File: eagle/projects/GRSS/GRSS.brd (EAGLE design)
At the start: 76 x 39 mm, 24 parts, among them J1 MOL-SL-2-RA, J10 MOL-SL-2-RA, J11 M02PTH, J2 MOL-SL-2-RA, J3 MOL-SL-2-RA, J4 MOL-SL-2-RA, J5 MOL-SL-2-RA, J6 MOL-SL-2-RA, J7 MOL-SL-2-RA, J8 MOL-SL-2-RA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

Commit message: board update rq
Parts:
- moved C2 9.49 mm to (60.8, 8.07)
- moved C3 9.06 mm to (60.7, 6.34)
- moved U2 3.00 mm to (66.1, 7.39)
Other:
- board size 76 x 39 mm -> 85 x 47 mm
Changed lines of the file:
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@@
 <board>
 <plain>
-<wire x1="0" y1="0" x2="76" y2="0" width="0" layer="20"/>
-<wire x1="76" y1="0" x2="76" y2="39" width="0" layer="20"/>
-<wire x1="76" y1="39" x2="0" y2="39" width="0" layer="20"/>
-<wire x1="0" y1="39" x2="0" y2="0" width="0" layer="20"/>
+<wire x1="0" y1="0" x2="85" y2="0" width="0" layer="20"/>
+<wire x1="85" y1="0" x2="85" y2="47" width="0" layer="20"/>
+<wire x1="85" y1="47" x2="0" y2="47" width="0" layer="20"/>
+<wire x1="0" y1="47" x2="0" y2="0" width="0" layer="20"/>
 </plain>
 <attributes>
@@
 <attribute name="TOLERANCE" value="10%" x="69.704" y="25.944" size="1.778" layer="27" display="off"/>
 </element>
-<element name="C2" library="grss" package="C0603" value="10uF" x="69.756" y="5.072">
-<attribute name="VENDOR_PN" value="490-10474-1-ND" x="69.756" y="5.072" size="1.778" layer="27" display="off"/>
-<attribute name="VENDOR" value="Digi-key" x="69.756" y="5.072" size="1.778" layer="27" display="off"/>
-<attribute name="MANUFACTURER" value="Murata" x="69.756" y="5.072" size="1.778" layer="27" display="off"/>
-<attribute name="VOLTAGE" value="10V" x="69.756" y="5.072" size="1.778" layer="27" display="off"/>
-<attribute name="MANUFACTURER_PN" value="GRM188R61A106KE69D" x="69.756" y="5.072" size="1.778" layer="27" display="off"/>
-<attribute name="TEMP_COEFF" value="X5R" x="69.756" y="5.072" size="1.778" layer="27" display="off"/>
-<attribute name="TOLERANCE" value="10%" x="69.756" y="5.072" size="1.778" layer="27" display="off"/>
-</element>
-<element name="C3" library="grss" package="C0603" value="2.2uF" x="69.74" y="7.342">
-<attribute name="VENDOR_PN" value="490-3296-1-ND" x="69.74" y="7.342" size="1.778" layer="27" display="off"/>
-<attribute name="VENDOR" value="Digi-key" x="69.74" y="7.342" size="1.778" layer="27" display="off"/>
-<attribute name="MANUFACTURER" value="Murata" x="69.74" y="7.342" size="1.778" layer="27" display="off"/>
-<attribute name="VOLTAGE" value="16V" x="69.74" y="7.342" size="1.778" layer="27" display="off"/>
-<attribute name="MANUFACTURER_PN" value="GRM188R61C225KE15D" x="69.74" y="7.342" size="1.778" layer="27" display="off"/>
-<attribute name="TEMP_COEFF" value="X5R" x="69.74" y="7.342" size="1.778" layer="27" display="off"/>
-<attribute name="TOLERANCE" value="10%" x="69.74" y="7.342" size="1.778" layer="27" display="off"/>
+<element name="C2" library="grss" package="C0603" value="10uF" x="60.756" y="8.072">
+<attribute name="VENDOR_PN" value="490-10474-1-ND" x="60.756" y="8.072" size="1.778" layer="27" display="off"/>
+<attribute name="VENDOR" value="Digi-key" x="60.756" y="8.072" size="1.778" layer="27" display="off"/>
+<attribute name="MANUFACTURER" value="Murata" x="60.756" y="8.072" size="1.778" layer="27" display="off"/>
+<attribute name="VOLTAGE" value="10V" x="60.756" y="8.072" size="1.778" layer="27" display="off"/>
+<attribute name="MANUFACTURER_PN" value="GRM188R61A106KE69D" x="60.756" y="8.072" size="1.778" layer="27" display="off"/>
+<attribute name="TEMP_COEFF" value="X5R" x="60.756" y="8.072" size="1.778" layer="27" display="off"/>
+<attribute name="TOLERANCE" value="10%" x="60.756" y="8.072" size="1.778" layer="27" display="off"/>
+</element>
+<element name="C3" library="grss" package="C0603" value="2.2uF" x="60.74" y="6.342">
+<attribute name="VENDOR_PN" value="490-3296-1-ND" x="60.74" y="6.342" size="1.778" layer="27" display="off"/>
+<attribute name="VENDOR" value="Digi-key" x="60.74" y="6.342" size="1.778" layer="27" display="off"/>
+<attribute name="MANUFACTURER" value="Murata" x="60.74" y="6.342" size="1.778" layer="27" display="off"/>
+<attribute name="VOLTAGE" value="16V" x="60.74" y="6.342" size="1.778" layer="27" display="off"/>
+<attribute name="MANUFACTURER_PN" value="GRM188R61C225KE15D" x="60.74" y="6.342" size="1.778" layer="27" display="off"/>
+<attribute name="TEMP_COEFF" value="X5R" x="60.74" y="6.342" size="1.778" layer="27" display="off"/>
+<attribute name="TOLERANCE" value="10%" x="60.74" y="6.342" size="1.778" layer="27" display="off"/>
 </element>
 <element name="C4" library="grss" package="C0603" value="1uF" x="69.74" y="9.628">
@@
 <attribute name="TOLERANCE" value="1%" x="69.66" y="14.184" size="1.778" layer="27" display="off"/>
 </element>
-<element name="U2" library="grss" package="M08A" value="LMC555CMX/NOPB" x="63.09" y="7.39">
-<attribute name="VENDOR_PN" value="LMC555CMX/NOPBCT-ND" x="63.09" y="7.39" size="1.778" layer="27" display="off"/>
-<attribute name="VENDOR" value="Digi-key" x="63.09" y="7.39" size="1.778" layer="27" display="off"/>
-<attribute name="MANUFACTURER" value="Texas Instruments" x="63.09" y="7.39" size="1.778" layer="27" display="off"/>
-<attribute name="MANUFACTURER_PN" value="LMC555CMX/NOPB" x="63.09" y="7.39" size="1.778" layer="27" display="off"/>
+<element name="U2" library="grss" package="M08A" value="LMC555CMX/NOPB" x="66.09" y="7.39">
+<attribute name="VENDOR_PN" value="LMC555CMX/NOPBCT-ND" x="66.09" y="7.39" size="1.778" layer="27" display="off"/>
+<attribute name="VENDOR" value="Digi-key" x="66.09" y="7.39" size="1.778" layer="27" display="off"/>
+<attribute name="MANUFACTURER" value="Texas Instruments" x="66.09" y="7.39" size="1.778" layer="27" display="off"/>
+<attribute name="MANUFACTURER_PN" value="LMC555CMX/NOPB" x="66.09" y="7.39" size="1.778" layer="27" display="off"/>
 </element>
 <element name="U3" library="grss" package="MF05A" value="LP2985AIM5-4.5/NOPB" x="62.77" y="31.12">
@@
 <contactref element="U2" pad="8"/>
 <contactref element="U3" pad="5"/>
-<wire x1="65.5538" y1="9.295" x2="68.89" y2="7.342" width="0" layer="19" extent="1-1"/>
-<wire x1="65.5538" y1="8.025" x2="65.5538" y2="9.295" width="0" layer="19" extent="1-1"/>
-<wire x1="60.6262" y1="5.485" x2="65.5538" y2="8.025" width="0" layer="19" extent="1-1"/>
-<wire x1="70.51" y1="14.184" x2="65.5538" y2="9.295" width="0" layer="19" extent="1-1"/>
-<wire x1="63.9892" y1="32.0725" x2="60.6262" y2="5.485" width="0" layer="19" extent="1-1"/>
+<wire x1="68.5538" y1="9.295" x2="59.89" y2="6.342" width="0" layer="19" extent="1-1"/>
+<wire x1="68.5538" y1="8.025" x2="68.5538" y2="9.295" width="0" layer="19" extent="1-1"/>
+<wire x1="63.6262" y1="5.485" x2="68.5538" y2="8.025" width="0" layer="19" extent="1-1"/>
+<wire x1="70.51" y1="14.184" x2="68.5538" y2="9.295" width="0" layer="19" extent="1-1"/>
+<wire x1="63.9892" y1="32.0725" x2="63.6262" y2="5.485" width="0" layer="19" extent="1-1"/>
 <wire x1="68.854" y1="25.944" x2="63.9892" y2="32.0725" width="0" layer="19" extent="1-1"/>
 </signal>
@@
 <contactref element="U3" pad="2"/>
 <contactref element="Q1" pad="2"/>
-<wire x1="70.59" y1="7.342" x2="70.606" y2="5.072" width="0" layer="19" extent="1-1"/>
-<wire x1="70.59" y1="9.628" x2="70.59" y2="7.342" width="0" layer="19" extent="1-1"/>
+<wire x1="61.59" y1="6.342" x2="61.606" y2="8.072" width="0" layer="19" extent="1-1"/>
+<wire x1="70.59" y1="9.628" x2="61.59" y2="6.342" width="0" layer="19" extent="1-1"/>
 <wire x1="70.59" y1="11.66" x2="70.59" y2="9.628" width="0" layer="19" extent="1-1"/>
 <wire x1="65.39" y1="11.8213" x2="70.59" y2="9.628" width="0" layer="19" extent="1-1"/>
-<wire x1="60.6262" y1="9.295" x2="70.59" y2="11.66" width="0" layer="19" extent="1-1"/>
-<wire x1="61.5508" y1="31.12" x2="60.6262" y2="9.295" width="0" layer="19" extent="1-1"/>
+<wire x1="63.6262" y1="9.295" x2="70.59" y2="11.66" width="0" layer="19" extent="1-1"/>
+<wire x1="61.5508" y1="31.12" x2="63.6262" y2="9.295" width="0" layer="19" extent="1-1"/>
 <wire x1="70.554" y1="25.944" x2="61.5508" y2="31.12" width="0" layer="19" extent="1-1"/>
 <wire x1="56.506" y1="11.922" x2="65.39" y2="11.8213" width="0" layer="19" extent="1-1"/>
@@
 <contactref element="U2" pad="2"/>
 <contactref element="U2" pad="6"/>
-<wire x1="65.5538" y1="6.755" x2="68.906" y2="5.072" width="0" layer="19" extent="1-1"/>
-<wire x1="60.6262" y1="8.025" x2="65.5538" y2="6.755" width="0" layer="19" extent="1-1"/>
-<wire x1="68.81" y1="14.184" x2="60.6262" y2="8.025" width="0" layer="19" extent="1-1"/>
+<wire x1="68.5538" y1="6.755" x2="59.906" y2="8.072" width="0" layer="19" extent="1-1"/>
+<wire x1="63.6262" y1="8.025" x2="68.5538" y2="6.755" width="0" layer="19" extent="1-1"/>
+<wire x1="68.81" y1="14.184" x2="63.6262" y2="8.025" width="0" layer="19" extent="1-1"/>
 </signal>
 <signal name="555OUT">
 <contactref element="U2" pad="3"/>
 <contactref element="Q1" pad="1"/>
-<wire x1="60.6262" y1="6.755" x2="60.89" y2="11.8213" width="0" layer="19" extent="1-1"/>
+<wire x1="63.6262" y1="6.755" x2="60.89" y2="11.8213" width="0" layer="19" extent="1-1"/>
 </signal>
 <signal name="VD">

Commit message: Tried an auto route for funzies
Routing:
- net 9V0: track 0.00 -> 103.0 mm
- net 4V5: track 0.00 -> 71.6 mm
- net GND: track 0.00 -> 67.0 mm, vias 0 -> 2
- net RES123: track 0.00 -> 49.3 mm
- net THRTRIG: track 0.00 -> 35.5 mm
- net VD: track 0.00 -> 25.1 mm
- net BP: track 0.00 -> 23.1 mm, vias 0 -> 2
- net LED78: track 0.00 -> 17.0 mm
- net LED89: track 0.00 -> 17.0 mm
- net RES456: track 0.00 -> 14.7 mm, vias 0 -> 1
- net 555OUT: track 0.00 -> 8.47 mm, vias 0 -> 2
- net LED45: track 0.00 -> 7.77 mm
- net LED23: track 0.00 -> 7.77 mm
- net LED12: track 0.00 -> 7.77 mm
- net LED56: track 0.00 -> 7.57 mm
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
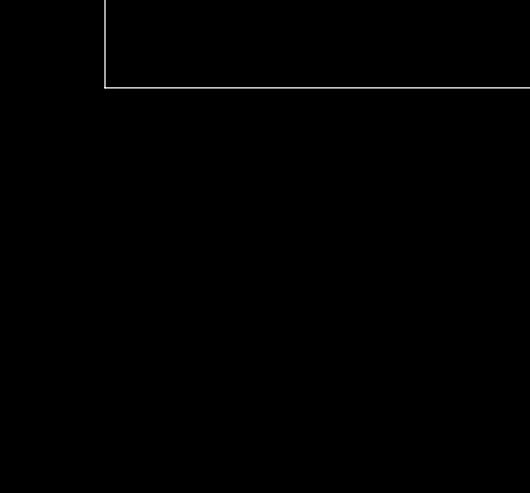
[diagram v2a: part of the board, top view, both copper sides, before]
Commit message: Added Test points / updated desc on 555 Timer
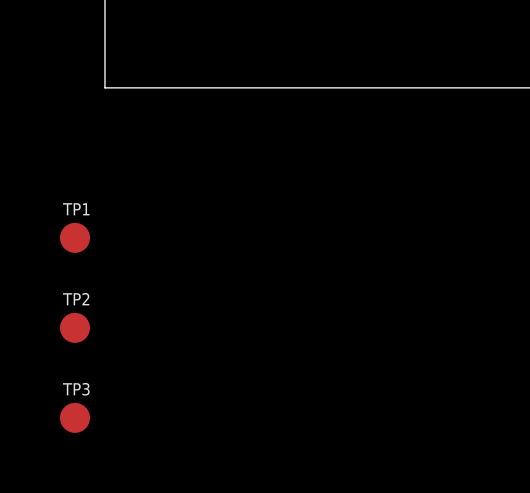
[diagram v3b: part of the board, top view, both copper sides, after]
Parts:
- added TP1, TP2, TP3: (no value), grss:TP10R
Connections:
- net 4V5: now also TP1.TP
- net 555OUT: now also TP2.TP
- net VD: now also TP3.TP
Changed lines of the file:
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@@
 <attribute name="MANUFACTURER_PN" value="LP2985AIM5-4.5/NOPB" x="62.77" y="31.12" size="1.778" layer="27" display="off"/>
+</element>
+<element name="TP1" library="grss" package="TP10R" value="" x="-1" y="-5">
+<attribute name="TP_SIGNAL_NAME" value="" x="-1" y="-5" size="1.778" layer="27" display="off"/>
+</element>
+<element name="TP2" library="grss" package="TP10R" value="" x="-1" y="-8">
+<attribute name="TP_SIGNAL_NAME" value="" x="-1" y="-8" size="1.778" layer="27" display="off"/>
+</element>
+<element name="TP3" library="grss" package="TP10R" value="" x="-1" y="-11">
+<attribute name="TP_SIGNAL_NAME" value="" x="-1" y="-11" size="1.778" layer="27" display="off"/>
 </element>
 </elements>
@@
 <wire x1="68.58" y1="8.001" x2="68.5538" y2="8.025" width="0.254" layer="1"/>
 <wire x1="63.7794" y1="5.2578" x2="63.6262" y2="5.485" width="0.254" layer="1"/>
+<contactref element="TP1" pad="TP"/>
 <wire x1="67.8942" y1="8.6868" x2="68.5538" y2="9.295" width="0" layer="19" extent="1-1"/>
+<wire x1="-1" y1="-5" x2="54.1782" y2="9.8298" width="0" layer="19" extent="1-1"/>
 </signal>
 <signal name="BP">
@@
 <via x="62.4078" y="10.287" extent="1-16" drill="0.6096"/>
 <via x="65.3796" y="7.0866" extent="1-16" drill="0.6096"/>
+<contactref element="TP2" pad="TP"/>
+<wire x1="-1" y1="-8" x2="60.89" y2="11.8213" width="0" layer="19" extent="1-1"/>
 </signal>
 <signal name="VD">
@@
 <wire x1="68.58" y1="28.1178" x2="68.78" y2="28.153" width="0.254" layer="1"/>
 <wire x1="63.3222" y1="18.0594" x2="63.14" y2="17.93" width="0.254" layer="1"/>
+<contactref element="TP3" pad="TP"/>
+<wire x1="-1" y1="-11" x2="63.14" y2="17.93" width="0" layer="19" extent="1-1"/>
 </signal>
 <signal name="RES789">

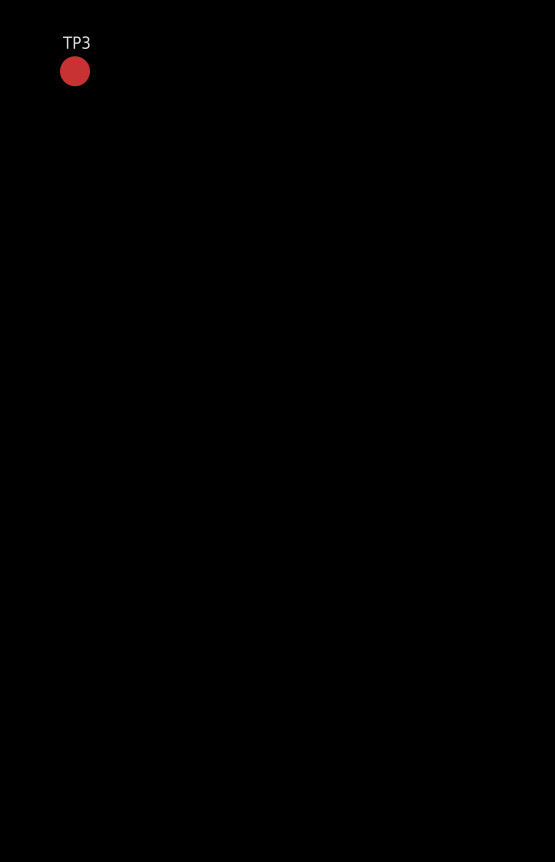
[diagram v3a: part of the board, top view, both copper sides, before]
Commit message: added mounting holes to lib / sch
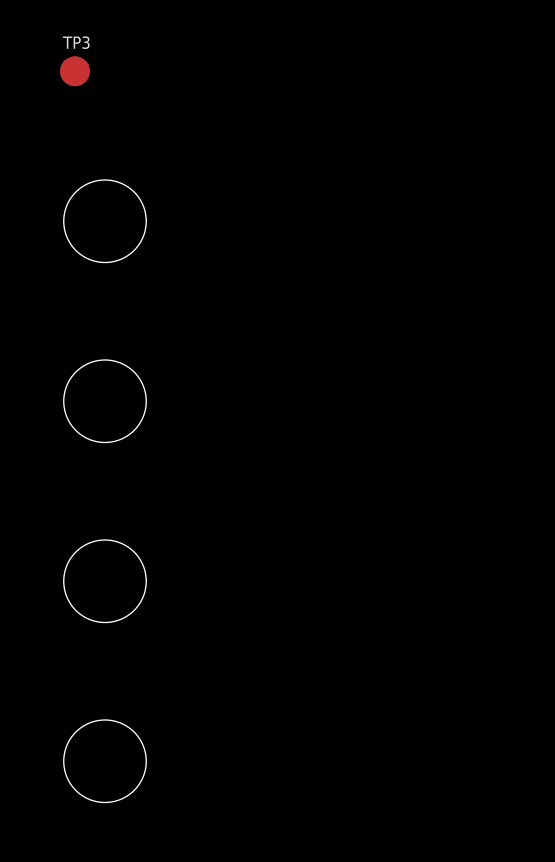
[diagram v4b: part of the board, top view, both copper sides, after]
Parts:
- added H1, H2, H3, H4: MOUNT-HOLE_2.75, grss:2,75_HOLE_RASPI
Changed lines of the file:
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@@
 <attribute name="TP_SIGNAL_NAME" value="" x="-1" y="-11" size="1.778" layer="27" display="off"/>
 </element>
+<element name="H1" library="grss" package="2,75_HOLE_RASPI" value="MOUNT-HOLE_2.75" x="0" y="-16"/>
+<element name="H2" library="grss" package="2,75_HOLE_RASPI" value="MOUNT-HOLE_2.75" x="0" y="-22"/>
+<element name="H3" library="grss" package="2,75_HOLE_RASPI" value="MOUNT-HOLE_2.75" x="0" y="-28"/>
+<element name="H4" library="grss" package="2,75_HOLE_RASPI" value="MOUNT-HOLE_2.75" x="0" y="-34"/>
 </elements>
 <signals>

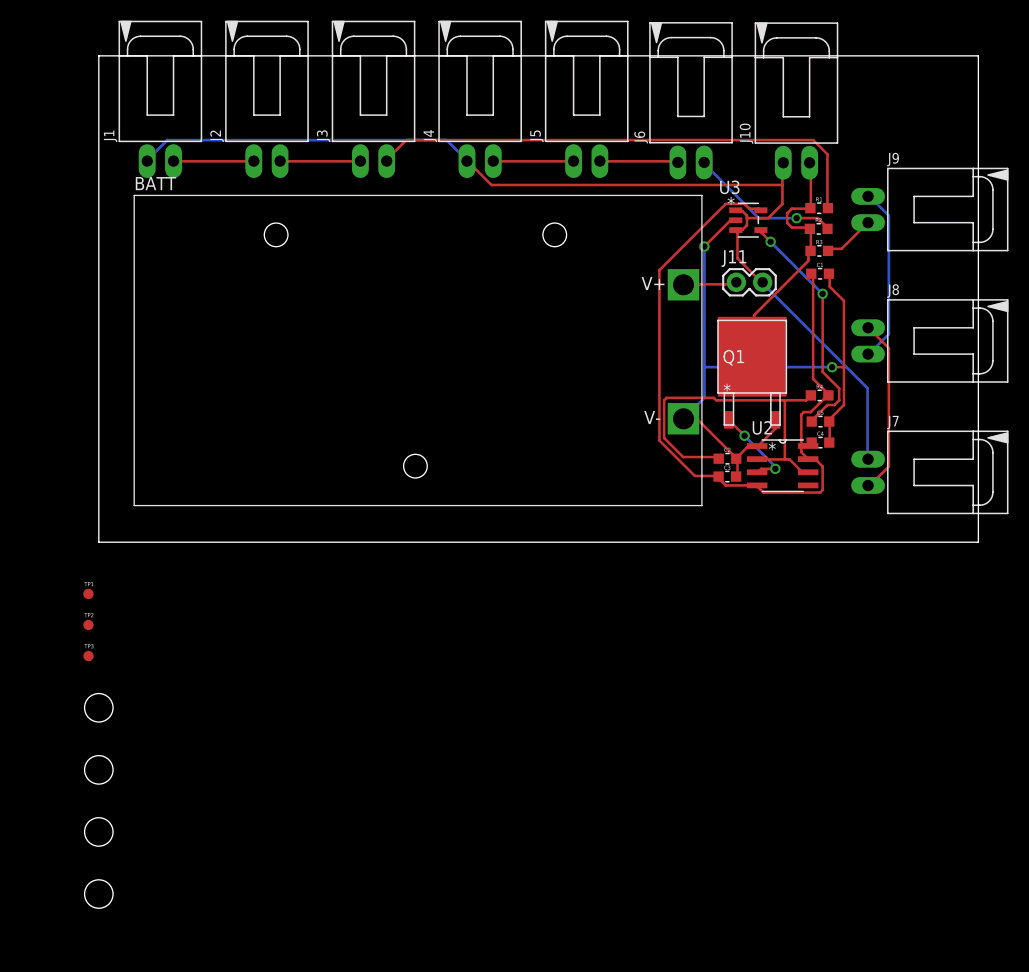
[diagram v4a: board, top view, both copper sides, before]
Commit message: Updated Resistors to be 0805 and added 3 0805 res to Lib
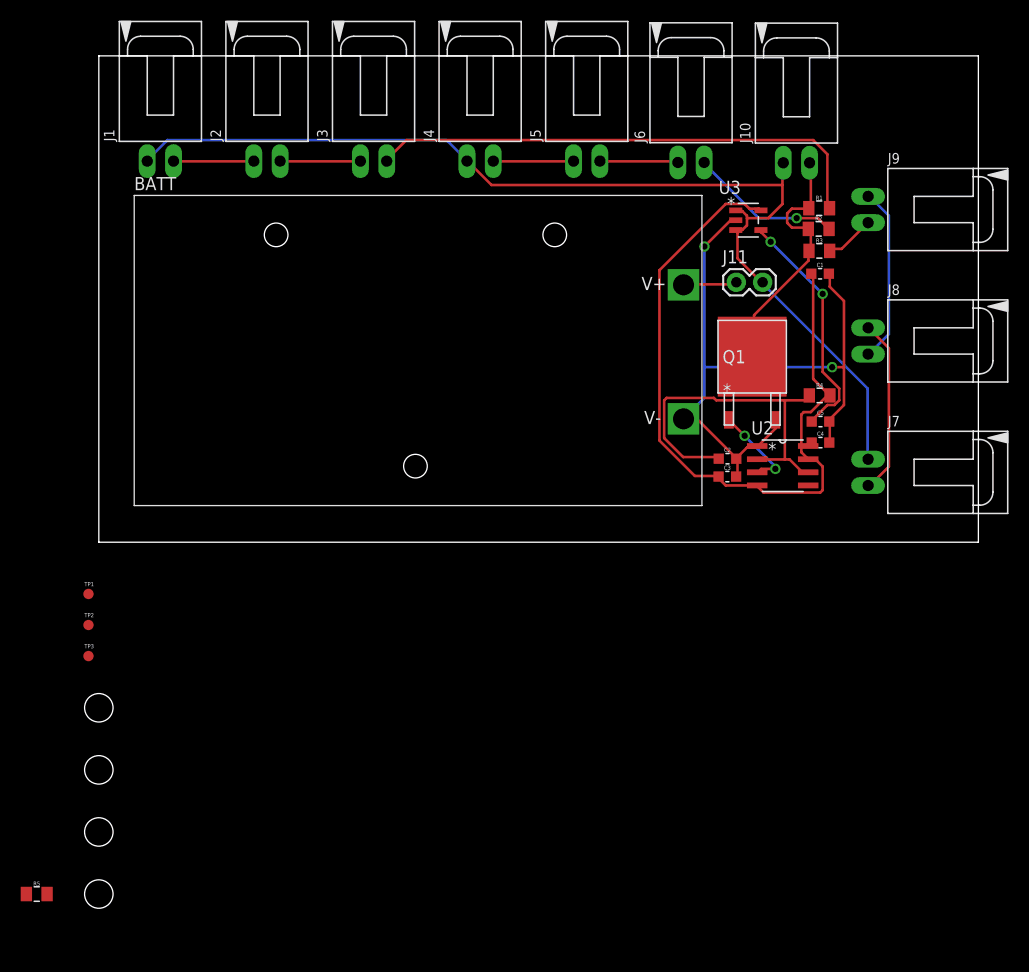
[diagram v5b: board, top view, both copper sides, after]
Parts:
- added R5: 4.7k, grss:R0805
- R1, R2, R3, R4: device grss:R0603 -> grss:R0805
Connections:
- net 555OUT: now also R5.2
- net GND: now also R5.1
